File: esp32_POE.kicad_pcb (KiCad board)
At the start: 4 copper layers, 150.1 x 40 mm, 83 parts, among them J1 Barrel_Jack_Switch, J2 Conn_02x03_Odd_Even, J3 Conn_01x04, J4 Conn_01x04, J5 Conn_01x03, J6 Conn_01x03, J7 Conn_01x03, J8 Conn_01x03, SW1 SW_Push, SW2 SW_Push, U1 HY931147C, U2 TPS2372, U3 TPS54560BDDA, U4 LAN8720A, U5 SN74LVC8T245, U6 ESP32-WROOM-32E, U7 XC6206PxxxMR

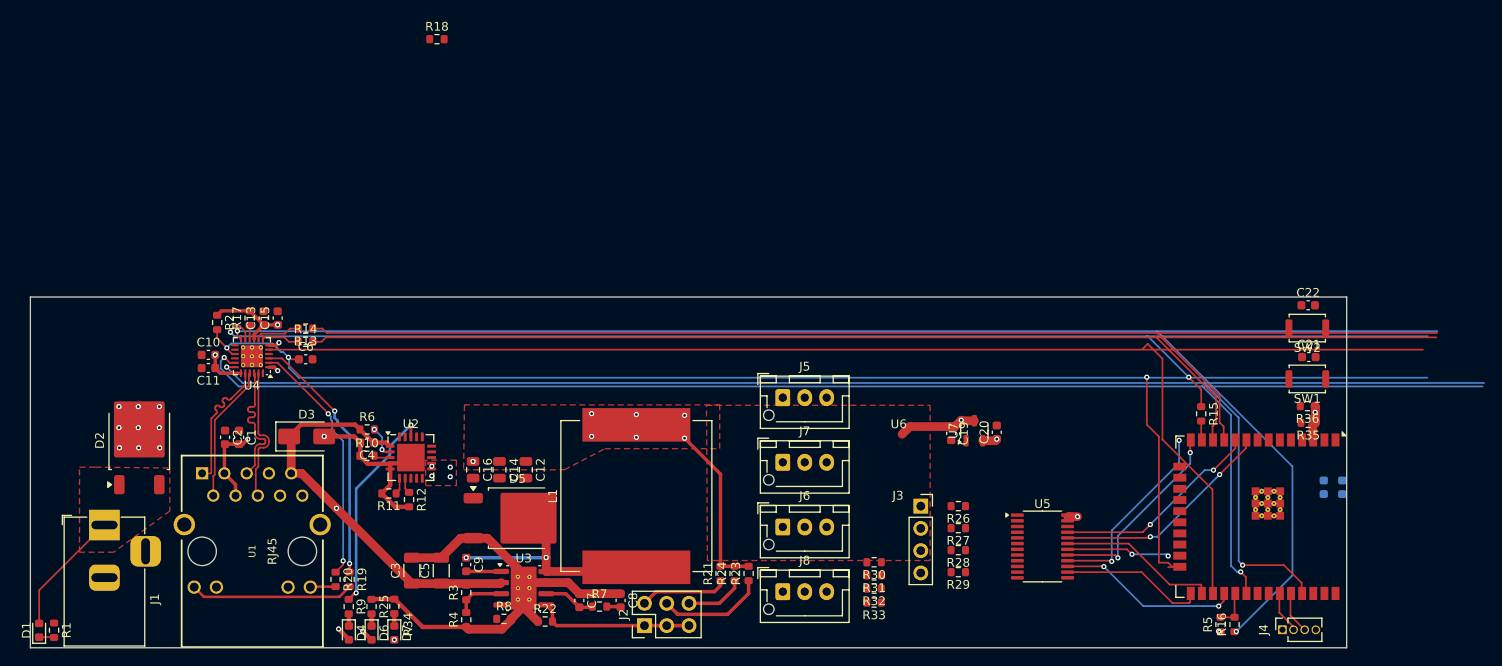
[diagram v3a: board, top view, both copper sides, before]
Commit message: Finished 1st routing pass, reduced size of PCB
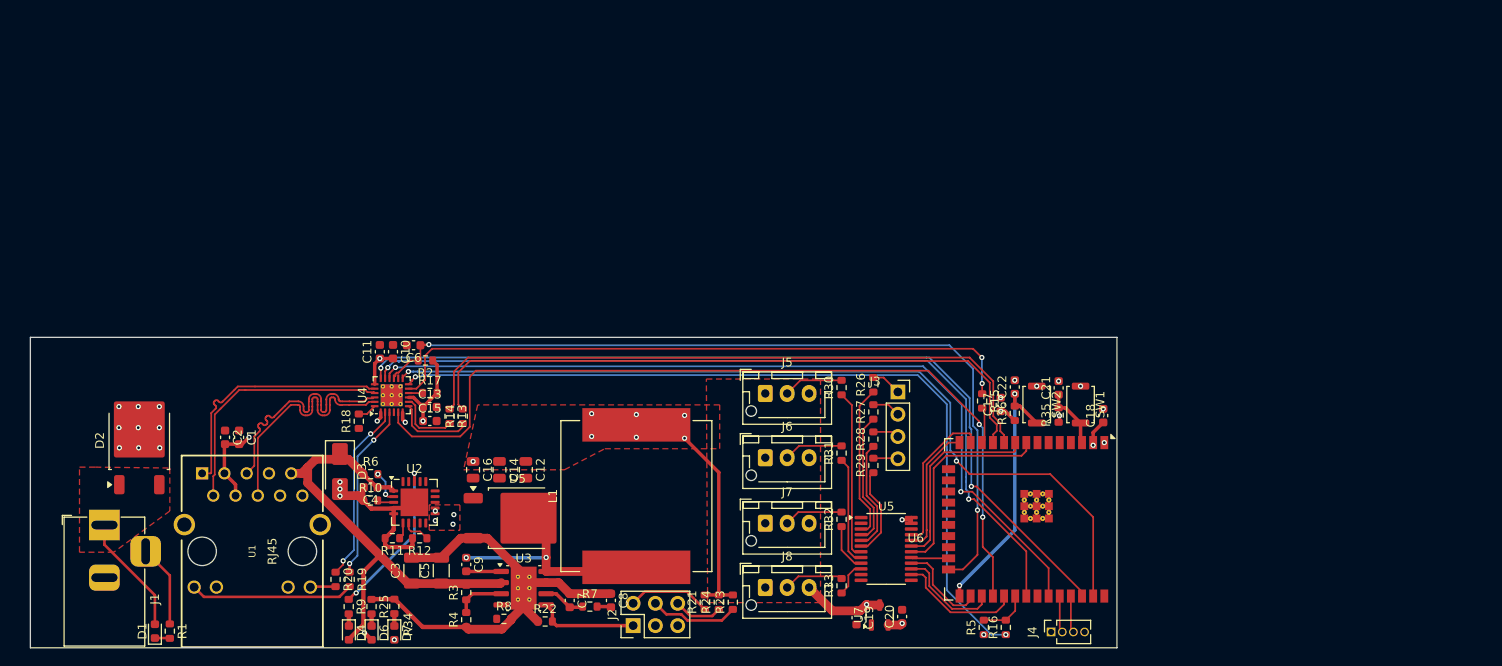
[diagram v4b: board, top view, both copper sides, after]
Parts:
- C17, C18: moved to F.Cu
- R26, R27, R28, R29, R30, R31, R32, R33: value 10 -> 120
- moved R18 44.5 mm to (119.3, 118.2), turned to 90 degrees
- moved C17 38.0 mm to (192.5, 116.2), turned to 90 degrees
- moved C22 34.7 mm to (194.2, 114.3), turned to 90 degrees
- moved R36 33.4 mm to (194.2, 117.3), turned to 90 degrees
- moved SW2 32.1 mm to (196.7, 116.3), turned to -90 degrees
- moved C21 28.7 mm to (199.2, 114.4), turned to 90 degrees
- moved R35 28.5 mm to (199.2, 117.5), turned to 90 degrees
- moved C18 28.5 mm to (204.2, 117.5), turned to 90 degrees
- moved R5 27.0 mm to (190.6, 141.7)
- moved U6 26.4 mm to (199.1, 129.3)
- moved J4 26.4 mm to (198.3, 142.2)
- moved R16 26.1 mm to (193.1, 141.7)
- moved SW1 26.0 mm to (201.7, 116.3), turned to -90 degrees
- moved R15 25.0 mm to (190.4, 115.8)
- moved R2 24.1 mm to (127.0, 111.2), turned to 180 degrees
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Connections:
- J4 pad 4: VCC -> +3.3V
- U6 pad 13: /CHANNEL4 -> /CHANNEL8
- U6 pad 14: /CHANNEL3 -> /CHANNEL7
- U6 pad 23: /CHANNEL5 -> /CHANNEL4
- U6 pad 26: /CHANNEL1 -> /CHANNEL3
- U6 pad 27: /CHANNEL6 -> /CHANNEL2
- U6 pad 29: /CHANNEL2 -> /CHANNEL1
- U6 pad 8: /CHANNEL7 -> /CHANNEL5
- U6 pad 9: /CHANNEL8 -> /CHANNEL6
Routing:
- net /ETH_MDC: track 0.00 -> 98.7 mm, vias 0 -> 2
- net /ETH_TXDEN: track 0.00 -> 94.7 mm, vias 0 -> 2
- net Net-(U4-MDIO): track 181.5 -> 93.3 mm
- net /ETH_TXD0: track 173.7 -> 95.1 mm
- net /ETH_TXD1: track 176.6 -> 99.1 mm
- net Net-(U4-CRS_DV/MODE2): track 150.6 -> 73.6 mm
- net /ETH_RST: track 168.6 -> 96.2 mm, vias 3 -> 2
- net /ETH_RXD1: track 143.2 -> 73.9 mm
- net /ETH_RXD0: track 143.9 -> 75.3 mm
- net /ETH_CLK: track 164.0 -> 97.5 mm, vias 0 -> 2
- net IO0: track 0.00 -> 30.4 mm, vias 0 -> 2
- net /5V_CHANNEL4: track 0.00 -> 19.3 mm
- net /CHANNEL4: track 22.7 -> 4.29 mm, vias 2 -> 0
- net /5V_CHANNEL8: track 0.00 -> 17.6 mm
- net /5V_CHANNEL7: track 0.00 -> 15.2 mm
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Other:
- board size 150.1 x 40 mm -> 123.9 x 35.4 mm
- board text added: "ik they don't have to be length-matched"
